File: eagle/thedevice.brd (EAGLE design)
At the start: 101.6 x 57.1 mm, 53 parts, among them J1 SBH11-PBPC-D10, J2 SBH11-PBPC-D12, U1 ADXL345, U2 BMP180, U3 HTU21DSMD, U4 LSM9DS0, U5 SPI_FLASH-X25XXSMD, U6 LTC3426, U7 LTC3426, X1 molex

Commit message: made all changes for V1.1
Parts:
- removed C11, C13: 10uF, SparkFun-Capacitors:0603-CAP
- removed C12, C14: 100nF, SparkFun-Capacitors:0603-CAP
- removed JP2: (no value), SparkFun-Connectors:1X04
- removed U1: ADXL345, SparkFun:LGA14
- removed U5: SPI_FLASH-X25XXSMD, SparkFun-DigitalIC:SO08
- added JP3: M02PTH, SparkFun-Connectors:1X02
- added R15: (no value), SparkFun-Passives:0603-RES
- added S3: (no value), SparkFun-Electromechanical:SWITCH-SPDT-SMD
- added U$17: SPI_FLASH-X25XXSMD1, SparkFun-DigitalIC:SO08-EIAJ
- added U$28: M08X2, SparkFun-Connectors:2X8
- JP1: value 2X6 FEMALE -> (none); device SparkFun-Connectors:2X6 -> SparkFun-Connectors:1X05_NO_SILK
- moved BAT1 58.5 mm to (4.11, 53.8), turned to 270 degrees
- moved JP1 55.5 mm to (44.6, 53.7), turned to 270 degrees
- moved D4 47.5 mm to (36.3, 8.51), turned to 90 degrees
- moved R5 33.1 mm to (74.6, 50.6), turned to 0 degrees
- moved R4 30.3 mm to (74.6, 48.3), turned to 0 degrees
- moved X1 12.5 mm to (51.2, 4.72), turned to 0 degrees
- moved R8 6.86 mm to (47.5, 12.1), turned to 180 degrees
- moved R7 5.66 mm to (51.5, 12.1), turned to 0 degrees
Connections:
- removed net ADXLINT1: J2.5, U1.8
- removed net ADXLINT2: J2.3, U1.9
- removed net N$13: C14.2, U1.6
- new net N$11: D4.C, S3.2
- new net N$12: D4.A, JP3.2, R15.2
- new net N$15: U$28.4
- new net N$16: U$28.2
- new net UA10: J1.12, U$28.3
- new net UA8: J2.3, U$28.8
- new net UA9: J2.5, U$28.9
- net 3V3: now also J1.2, J2.2, J2.23, JP1.5, R6.2, U$17.3, U$17.7, U$17.8, U$28.15; no longer C12.2, JP1.3, JP2.1, U1.1, U1.7, U5.3, U5.7, U5.8
- net 5V0: now also U$28.16; no longer JP1.1
- net ENABLE3V: no longer J1.12
- net FLASHCS: now also U$17.1; no longer U5.1
- net GND: now also U$17.4, U$28.6; no longer C11.1, C12.1, C13.1, C14.1, JP2.2, U1.12, U1.2, U1.4, U1.5, U5.4
- net N$3: now also JP3.1, R15.1; no longer D4.A
- net P4MISO: now also U$17.2; no longer U5.2
- net P4MOSI: now also U$17.5; no longer U5.5
- net P4SPICLK: now also U$17.6; no longer U5.6
- net SCL: now also JP1.2; no longer JP2.4, U1.14
- net SDA: now also JP1.1; no longer JP2.3, U1.13
- net UA0: now also U$28.5; no longer JP1.5
- net UA1: now also U$28.7; no longer JP1.7
- net UA2: now also U$28.1; no longer JP1.9
- net UA3: now also U$28.11; no longer JP1.11
- net UA4: now also U$28.13; no longer JP1.12
- net UA5: now also U$28.14; no longer JP1.10
- net UA6: now also U$28.12; no longer JP1.8
- net UA7: now also U$28.10; no longer JP1.6
- net VIN: now also S3.1; no longer D4.C, J1.2, J2.2, J2.23, JP1.2, R6.2
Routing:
- net VIN: track 142.8 -> 32.8 mm
- net UA10: track 0.00 -> 62.8 mm
- net UA9: track 0.00 -> 41.9 mm, vias 0 -> 2
- net UA8: track 0.00 -> 41.1 mm, vias 0 -> 1
- net GND: track 27.1 -> 2.29 mm, vias 131 -> 114
- net 3V3: track 174.0 -> 195.7 mm, vias 8 -> 5
- net N$3: track 4.13 -> 24.9 mm
- net UA2: track 41.5 -> 60.9 mm, vias 1 -> 0
- net ADXLINT1: track 15.7 -> 0.00 mm
- net QUADB: track 43.7 -> 28.1 mm
- net ENABLE3V: track 17.2 -> 2.60 mm
- net ADXLINT2: track 13.7 -> 0.00 mm
- net 5V0: track 96.5 -> 110.1 mm, vias 2 -> 1
- net LSM9DSOCSG: track 30.3 -> 17.1 mm, vias 5 -> 1
- net UA0: track 38.8 -> 45.2 mm, vias 0 -> 1
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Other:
- board text added: "3V 02 32 34 05 04 12 03"
- board text added: "5V 31 25 23 36 0V"
- board text added: "F = MA"
- board text added: "Newton's Attic"
- board text added: "Newtons Attic Physics Lab V1.1 Elkhorn Creek Engineering"
- board text added: "Physics Lab V1.1 Elkhorn Creek Engineering"
- board text removed: "Newtons Attic Physics Lab V1.0 Elkhorn Creek Engineering"

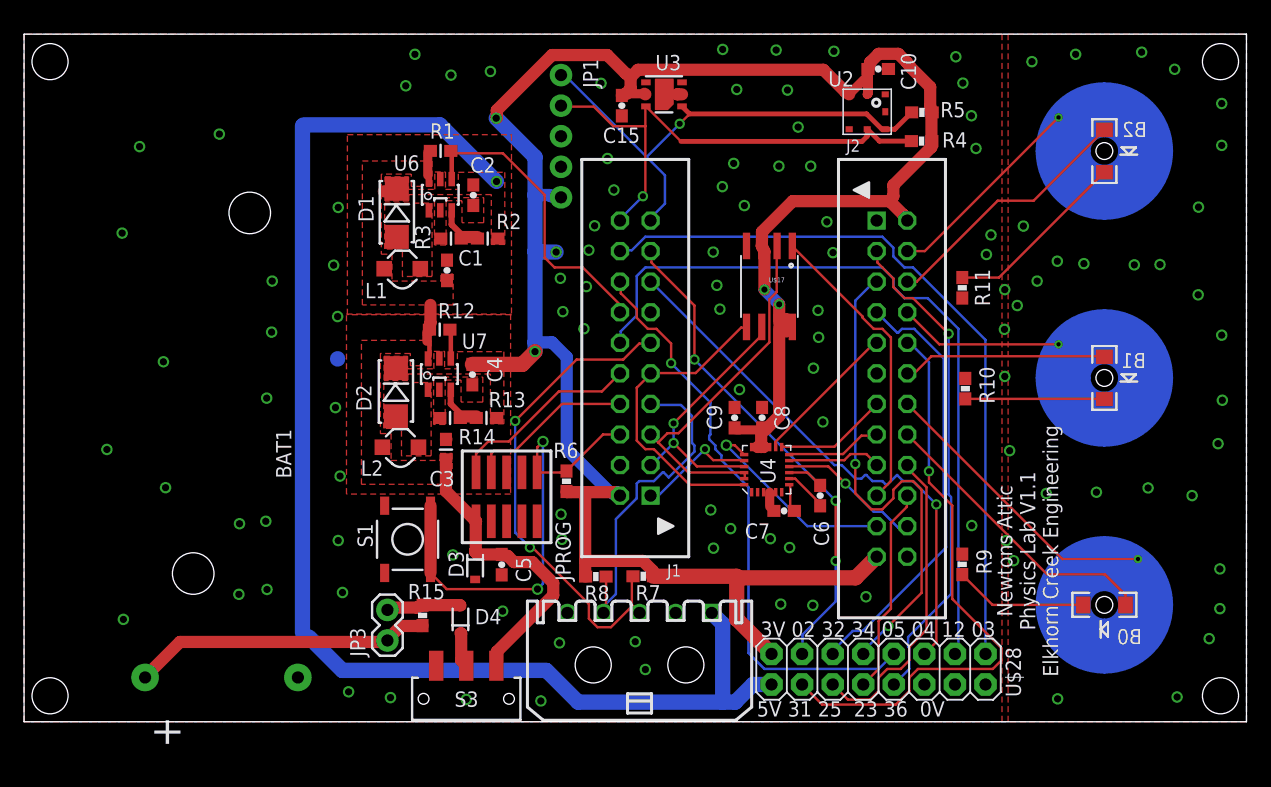
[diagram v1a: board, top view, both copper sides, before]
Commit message: Made all V1.2 changes except newtons laws
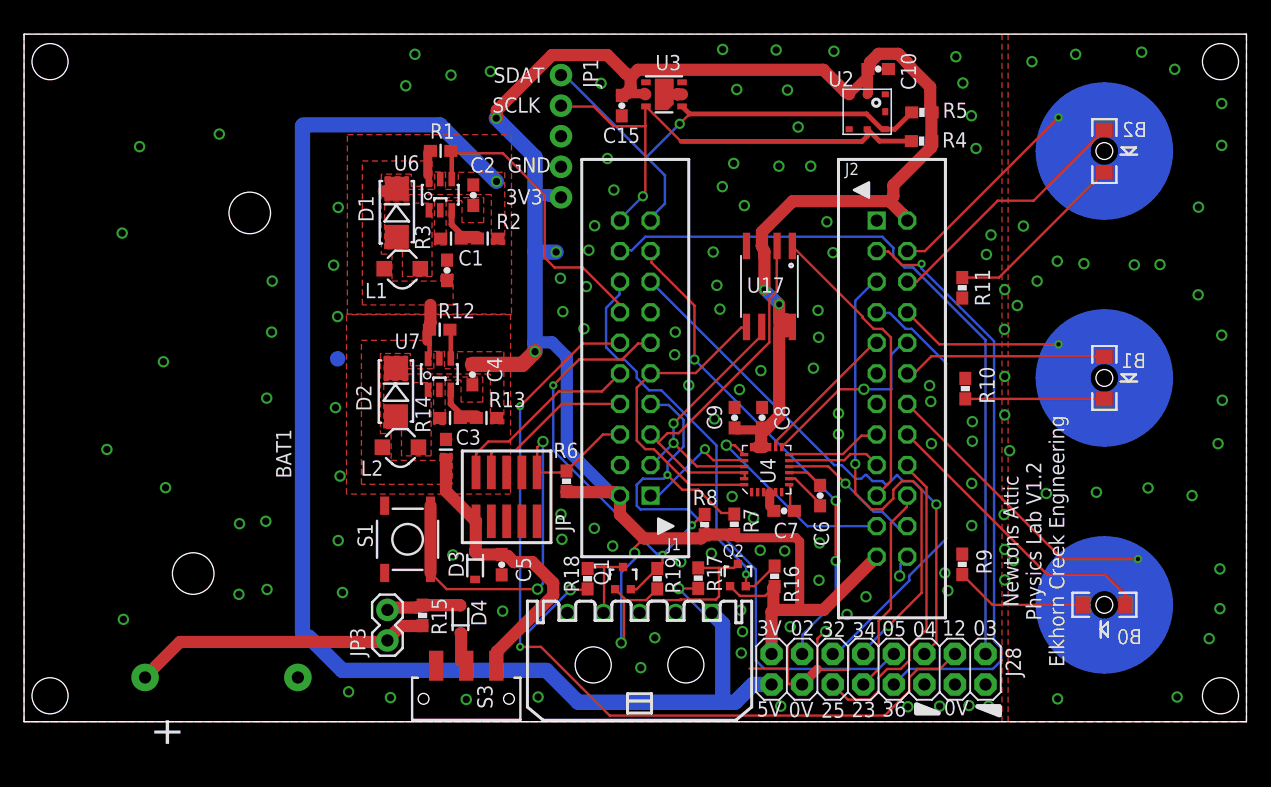
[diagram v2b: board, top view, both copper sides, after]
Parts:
- added Q1, Q2: MOSFET-NCHANNEL2N7002PW, SparkFun-DiscreteSemi:SOT323
- added R16, R17, R18, R19: 10k, SparkFun-Resistors:0603-RES
- moved R8 10.0 mm to (56.6, 16.4), turned to 270 degrees
- moved R7 8.71 mm to (59.0, 16.4), turned to 270 degrees
- renumbered JPROG to JP, U$17 to U17, U$28 to J28
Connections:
- removed net N$15: J28.4
- removed net N$16: J28.2
- removed net UA5: J2.10, J28.14
- new net N$14: Q2.3, R17.1, X1.P$3
- new net N$19: Q1.3, R18.1, X1.P$4
- net 3V3: now also Q1.1, Q2.1, R16.2, R19.2
- net 5V0: now also R17.2, R18.2
- net GND: now also J28.14, J28.2, J28.4
- net LSMINT1: now also J2.10; no longer J2.13
- net QUADA: now also Q1.2, R19.1, R8.1; no longer R7.1, X1.P$3
- net QUADB: now also Q2.2, R16.1, R7.1; no longer R8.1, X1.P$4
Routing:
- net UA5: track 49.2 -> 0.00 mm, vias 1 -> 0
- net 3V3: track 195.7 -> 216.8 mm, vias 5 -> 7
- net GND: track 2.29 -> 21.6 mm, vias 114 -> 145
- net 5V0: track 110.1 -> 124.9 mm, vias 1 -> 3
- net N$14: track 0.00 -> 13.0 mm
- net UA10: track 62.8 -> 71.8 mm, vias 0 -> 2
- net UA8: track 41.1 -> 49.7 mm
- net QUADB: track 28.1 -> 35.8 mm, vias 0 -> 2
- net N$19: track 0.00 -> 6.84 mm
- net LSMINT1: track 9.39 -> 15.7 mm, vias 0 -> 1
- net QUADA: track 41.1 -> 36.9 mm, vias 2 -> 3
- net UA1: track 48.9 -> 50.3 mm, vias 1 -> 0
- net UA3: track 36.4 -> 35.8 mm
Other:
- board text added: "02"
- board text added: "03"
- board text added: "04"
- board text added: "05"
- board text added: "0V"
- board text added: "12"
- board text added: "23"
- board text added: "25"
- board text added: "32"
- board text added: "34"
- board text added: "36"
- board text added: "3V"
- board text added: "3V3"
- board text added: "5V"
- board text added: "GND"
- board text added: "Newtons Attic Physics Lab V1.2 Elkhorn Creek Engineering"
- board text added: "Physics Lab V1.2 Elkhorn Creek Engineering"
- board text added: "SCLK"
- board text added: "SDAT"
- board text removed: "3V 02 32 34 05 04 12 03"
- board text removed: "5V 31 25 23 36 0V"
- board text removed: "Newton's Attic"
- board text removed: "Newtons Attic Physics Lab V1.1 Elkhorn Creek Engineering"
- board text removed: "Physics Lab V1.1 Elkhorn Creek Engineering"
